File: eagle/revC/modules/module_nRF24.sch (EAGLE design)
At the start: 10 parts

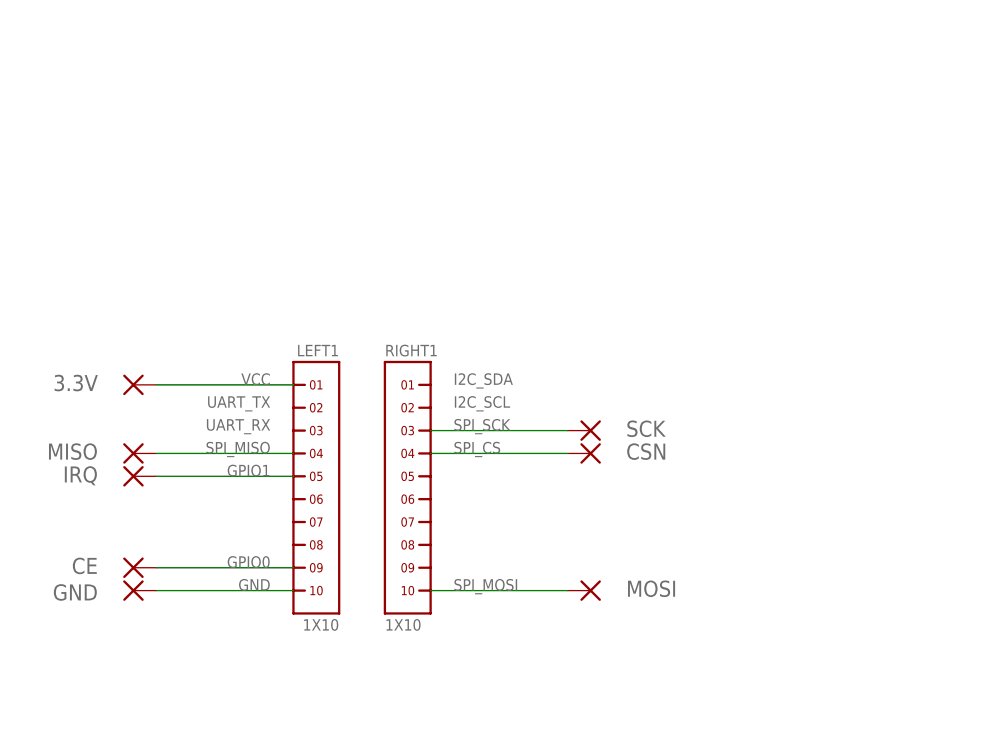
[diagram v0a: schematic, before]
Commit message: Replaced modules with library parts
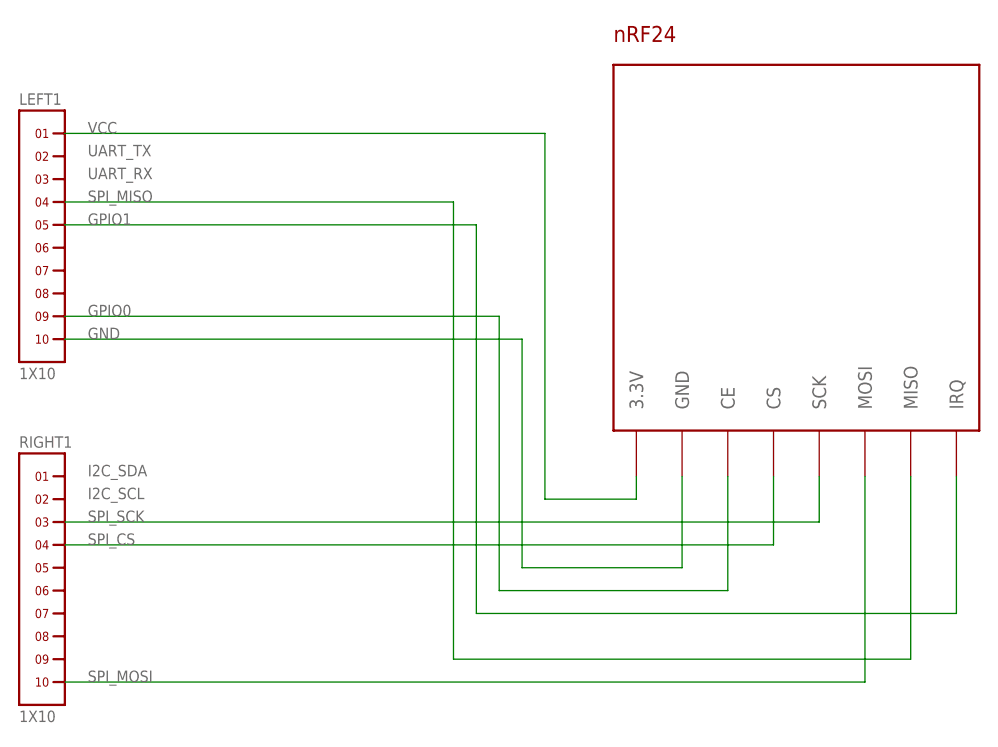
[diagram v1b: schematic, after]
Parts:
- removed 3.3V, CE, CSN, GND, IRQ, MISO, MOSI, SCK: (no value), wirepad:SMD1
- added U$1: NRF24, RadioShield:NRF24
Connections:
- net GND: now also U$1.GND; no longer GND.P
- net INT0: now also U$1.CE; no longer CE.P
- net INT1: now also U$1.IRQ; no longer IRQ.P
- net SPI_CS: now also U$1.CS; no longer CSN.P
- net SPI_MISO: now also U$1.MISO; no longer MISO.P
- net SPI_MOSI: now also U$1.MOSI; no longer MOSI.P
- net SPI_SCK: now also U$1.SCK; no longer SCK.P
- net VCC: now also U$1.3.3V; no longer 3.3V.P
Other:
- moved on the sheet: LEFT1, RIGHT1
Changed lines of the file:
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@@
 <?xml version="1.0" encoding="utf-8"?>
 <!DOCTYPE eagle SYSTEM "eagle.dtd">
-<eagle version="9.0.1">
+<eagle version="9.4.1">
 <drawing>
 <settings>
@@
 <part name="LEFT1" library="headers(2mm)" deviceset="1X10" device=""/>
 <part name="RIGHT1" library="headers(2mm)" deviceset="1X10" device=""/>
-<part name="SCK" library="wirepad" deviceset="SMD1" device=""/>
-<part name="CSN" library="wirepad" deviceset="SMD1" device=""/>
-<part name="GND" library="wirepad" deviceset="SMD1" device=""/>
-<part name="MOSI" library="wirepad" deviceset="SMD1" device=""/>
-<part name="3.3V" library="wirepad" deviceset="SMD1" device=""/>
-<part name="MISO" library="wirepad" deviceset="SMD1" device=""/>
-<part name="CE" library="wirepad" deviceset="SMD1" device=""/>
-<part name="IRQ" library="wirepad" deviceset="SMD1" device=""/>
+<part name="U$1" library="RadioShield" deviceset="NRF24" device=""/>
 </parts>
 <sheets>
 <sheet>
 <plain>
-<text x="33.02" y="40.64" size="1.27" layer="95" rot="MR0">VCC</text>
-<text x="33.02" y="38.1" size="1.27" layer="95" rot="MR0">UART_TX</text>
-<text x="33.02" y="35.56" size="1.27" layer="95" rot="MR0">UART_RX</text>
-<text x="33.02" y="33.02" size="1.27" layer="95" rot="MR0">SPI_MISO</text>
-<text x="33.02" y="30.48" size="1.27" layer="95" rot="MR0">GPIO1</text>
-<text x="33.02" y="17.78" size="1.27" layer="95" rot="MR0">GND</text>
-<text x="33.02" y="20.32" size="1.27" layer="95" rot="MR0">GPIO0</text>
-<text x="53.34" y="17.78" size="1.27" layer="95">SPI_MOSI</text>
-<text x="53.34" y="40.64" size="1.27" layer="95">I2C_SDA</text>
-<text x="53.34" y="38.1" size="1.27" layer="95">I2C_SCL</text>
-<text x="53.34" y="35.56" size="1.27" layer="95">SPI_SCK</text>
-<text x="53.34" y="33.02" size="1.27" layer="95">SPI_CS</text>
+<text x="12.7" y="68.58" size="1.27" layer="95">VCC</text>
+<text x="12.7" y="66.04" size="1.27" layer="95">UART_TX</text>
+<text x="12.7" y="63.5" size="1.27" layer="95">UART_RX</text>
+<text x="12.7" y="60.96" size="1.27" layer="95">SPI_MISO</text>
+<text x="12.7" y="58.42" size="1.27" layer="95">GPIO1</text>
+<text x="12.7" y="45.72" size="1.27" layer="95">GND</text>
+<text x="12.7" y="48.26" size="1.27" layer="95">GPIO0</text>
+<text x="12.7" y="7.62" size="1.27" layer="95">SPI_MOSI</text>
+<text x="12.7" y="30.48" size="1.27" layer="95">I2C_SDA</text>
+<text x="12.7" y="27.94" size="1.27" layer="95">I2C_SCL</text>
+<text x="12.7" y="25.4" size="1.27" layer="95">SPI_SCK</text>
+<text x="12.7" y="22.86" size="1.27" layer="95">SPI_CS</text>
 </plain>
 <instances>
-<instance part="LEFT1" gate="G$1" x="38.1" y="27.94" rot="MR0"/>
-<instance part="RIGHT1" gate="G$1" x="48.26" y="27.94"/>
-<instance part="SCK" gate="1" x="68.58" y="35.56" smashed="yes" rot="MR0">
-<attribute name="NAME" x="72.517" y="34.8742" size="1.778" layer="95"/>
-<attribute name="VALUE" x="69.723" y="32.258" size="1.778" layer="96" rot="MR0"/>
+<instance part="LEFT1" gate="G$1" x="7.62" y="55.88" smashed="yes">
+<attribute name="NAME" x="5.08" y="71.755" size="1.27" layer="95" font="vector"/>
+<attribute name="VALUE" x="5.08" y="41.275" size="1.27" layer="96" font="vector"/>
 </instance>
-<instance part="CSN" gate="1" x="68.58" y="33.02" smashed="yes" rot="MR0">
-<attribute name="NAME" x="72.517" y="32.3342" size="1.778" layer="95"/>
-<attribute name="VALUE" x="69.723" y="29.718" size="1.778" layer="96" rot="MR0"/>
+<instance part="RIGHT1" gate="G$1" x="7.62" y="17.78" smashed="yes">
+<attribute name="NAME" x="5.08" y="33.655" size="1.27" layer="95" font="vector"/>
+<attribute name="VALUE" x="5.08" y="3.175" size="1.27" layer="96" font="vector"/>
 </instance>
-<instance part="GND" gate="1" x="17.78" y="17.78" smashed="yes" rot="MR180">
-<attribute name="NAME" x="13.843" y="18.4658" size="1.778" layer="95" rot="R180"/>
-<attribute name="VALUE" x="16.637" y="21.082" size="1.778" layer="96" rot="MR180"/>
-</instance>
-<instance part="MOSI" gate="1" x="68.58" y="17.78" smashed="yes" rot="MR0">
-<attribute name="NAME" x="72.517" y="17.0942" size="1.778" layer="95"/>
-<attribute name="VALUE" x="69.723" y="14.478" size="1.778" layer="96" rot="MR0"/>
-</instance>
-<instance part="3.3V" gate="1" x="17.78" y="40.64" smashed="yes">
-<attribute name="NAME" x="13.843" y="39.9542" size="1.778" layer="95" rot="MR0"/>
-<attribute name="VALUE" x="16.637" y="37.338" size="1.778" layer="96"/>
-</instance>
-<instance part="MISO" gate="1" x="17.78" y="33.02" smashed="yes">
-<attribute name="NAME" x="13.843" y="32.3342" size="1.778" layer="95" rot="MR0"/>
-<attribute name="VALUE" x="16.637" y="29.718" size="1.778" layer="96"/>
-</instance>
-<instance part="CE" gate="1" x="17.78" y="20.32" smashed="yes">
-<attribute name="NAME" x="13.843" y="19.6342" size="1.778" layer="95" rot="MR0"/>
-<attribute name="VALUE" x="16.637" y="17.018" size="1.778" layer="96"/>
-</instance>
-<instance part="IRQ" gate="1" x="17.78" y="30.48" smashed="yes">
-<attribute name="NAME" x="13.843" y="29.7942" size="1.778" layer="95" rot="MR0"/>
-<attribute name="VALUE" x="16.637" y="27.178" size="1.778" layer="96"/>
-</instance>
+<instance part="U$1" gate="G$1" x="91.44" y="55.88" smashed="yes"/>
 </instances>
 <busses>
@@
 <segment>
 <pinref part="LEFT1" gate="G$1" pin="1"/>
-<wire x1="35.56" y1="40.64" x2="20.32" y2="40.64" width="0.1524" layer="91"/>
-<pinref part="3.3V" gate="1" pin="P"/>
+<wire x1="10.16" y1="68.58" x2="63.5" y2="68.58" width="0.1524" layer="91"/>
+<wire x1="63.5" y1="68.58" x2="63.5" y2="27.94" width="0.1524" layer="91"/>
+<wire x1="63.5" y1="27.94" x2="73.66" y2="27.94" width="0.1524" layer="91"/>
+<pinref part="U$1" gate="G$1" pin="3.3V"/>
+<wire x1="73.66" y1="27.94" x2="73.66" y2="30.48" width="0.1524" layer="91"/>
 </segment>
 </net>
@@
 <segment>
 <pinref part="LEFT1" gate="G$1" pin="4"/>
-<wire x1="35.56" y1="33.02" x2="20.32" y2="33.02" width="0.1524" layer="91"/>
-<pinref part="MISO" gate="1" pin="P"/>
+<wire x1="10.16" y1="60.96" x2="53.34" y2="60.96" width="0.1524" layer="91"/>
+<wire x1="53.34" y1="60.96" x2="53.34" y2="10.16" width="0.1524" layer="91"/>
+<pinref part="U$1" gate="G$1" pin="MISO"/>
+<wire x1="53.34" y1="10.16" x2="104.14" y2="10.16" width="0.1524" layer="91"/>
+<wire x1="104.14" y1="10.16" x2="104.14" y2="30.48" width="0.1524" layer="91"/>
 </segment>
 </net>
@@
 <segment>
 <pinref part="LEFT1" gate="G$1" pin="9"/>
-<wire x1="35.56" y1="20.32" x2="20.32" y2="20.32" width="0.1524" layer="91"/>
-<pinref part="CE" gate="1" pin="P"/>
+<wire x1="10.16" y1="48.26" x2="58.42" y2="48.26" width="0.1524" layer="91"/>
+<wire x1="58.42" y1="48.26" x2="58.42" y2="17.78" width="0.1524" layer="91"/>
+<pinref part="U$1" gate="G$1" pin="CE"/>
+<wire x1="58.42" y1="17.78" x2="83.82" y2="17.78" width="0.1524" layer="91"/>
+<wire x1="83.82" y1="17.78" x2="83.82" y2="30.48" width="0.1524" layer="91"/>
 </segment>
 </net>
@@
 <segment>
 <pinref part="RIGHT1" gate="G$1" pin="10"/>
-<wire x1="50.8" y1="17.78" x2="66.04" y2="17.78" width="0.1524" layer="91"/>
-<pinref part="MOSI" gate="1" pin="P"/>
+<pinref part="U$1" gate="G$1" pin="MOSI"/>
+<wire x1="10.16" y1="7.62" x2="99.06" y2="7.62" width="0.1524" layer="91"/>
+<wire x1="99.06" y1="7.62" x2="99.06" y2="30.48" width="0.1524" layer="91"/>
 </segment>
 </net>
@@
 <segment>
 <pinref part="RIGHT1" gate="G$1" pin="3"/>
-<wire x1="50.8" y1="35.56" x2="66.04" y2="35.56" width="0.1524" layer="91"/>
-<pinref part="SCK" gate="1" pin="P"/>
+<pinref part="U$1" gate="G$1" pin="SCK"/>
+<wire x1="10.16" y1="25.4" x2="93.98" y2="25.4" width="0.1524" layer="91"/>
+<wire x1="93.98" y1="25.4" x2="93.98" y2="30.48" width="0.1524" layer="91"/>
 </segment>
 </net>
@@
 <segment>
 <pinref part="RIGHT1" gate="G$1" pin="4"/>
-<wire x1="50.8" y1="33.02" x2="66.04" y2="33.02" width="0.1524" layer="91"/>
-<pinref part="CSN" gate="1" pin="P"/>
+<pinref part="U$1" gate="G$1" pin="CS"/>
+<wire x1="10.16" y1="22.86" x2="88.9" y2="22.86" width="0.1524" layer="91"/>
+<wire x1="88.9" y1="22.86" x2="88.9" y2="30.48" width="0.1524" layer="91"/>
 </segment>
 </net>
@@
 <segment>
 <pinref part="LEFT1" gate="G$1" pin="10"/>
-<wire x1="20.32" y1="17.78" x2="35.56" y2="17.78" width="0.1524" layer="91"/>
-<pinref part="GND" gate="1" pin="P"/>
+<wire x1="10.16" y1="45.72" x2="60.96" y2="45.72" width="0.1524" layer="91"/>
+<wire x1="60.96" y1="45.72" x2="60.96" y2="20.32" width="0.1524" layer="91"/>
+<pinref part="U$1" gate="G$1" pin="GND"/>
+<wire x1="60.96" y1="20.32" x2="78.74" y2="20.32" width="0.1524" layer="91"/>
+<wire x1="78.74" y1="20.32" x2="78.74" y2="30.48" width="0.1524" layer="91"/>
 </segment>
 </net>
 <net name="INT1" class="0">
 <segment>
-<pinref part="IRQ" gate="1" pin="P"/>
 <pinref part="LEFT1" gate="G$1" pin="5"/>
-<wire x1="20.32" y1="30.48" x2="35.56" y2="30.48" width="0.1524" layer="91"/>
-</segment>
-</net>
+<wire x1="10.16" y1="58.42" x2="55.88" y2="58.42" width="0.1524" layer="91"/>
+<wire x1="55.88" y1="58.42" x2="55.88" y2="15.24" width="0.1524" layer="91"/>
+<pinref part="U$1" gate="G$1" pin="IRQ"/>
+<wire x1="55.88" y1="15.24" x2="109.22" y2="15.24" width="0.1524" layer="91"/>
+<wire x1="109.22" y1="15.24" x2="109.22" y2="30.48" width="0.1524" layer="91"/>
+</segment>
+</net>
